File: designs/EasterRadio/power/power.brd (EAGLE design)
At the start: 30.5 x 44.5 mm, 23 parts, among them IC1 MCP73832T-2ACI_OT, IC2 TPS62160DGKR, IC3 DMP1045U-7, J1 10118192-0001LF, J2 S2B-PH-SM4

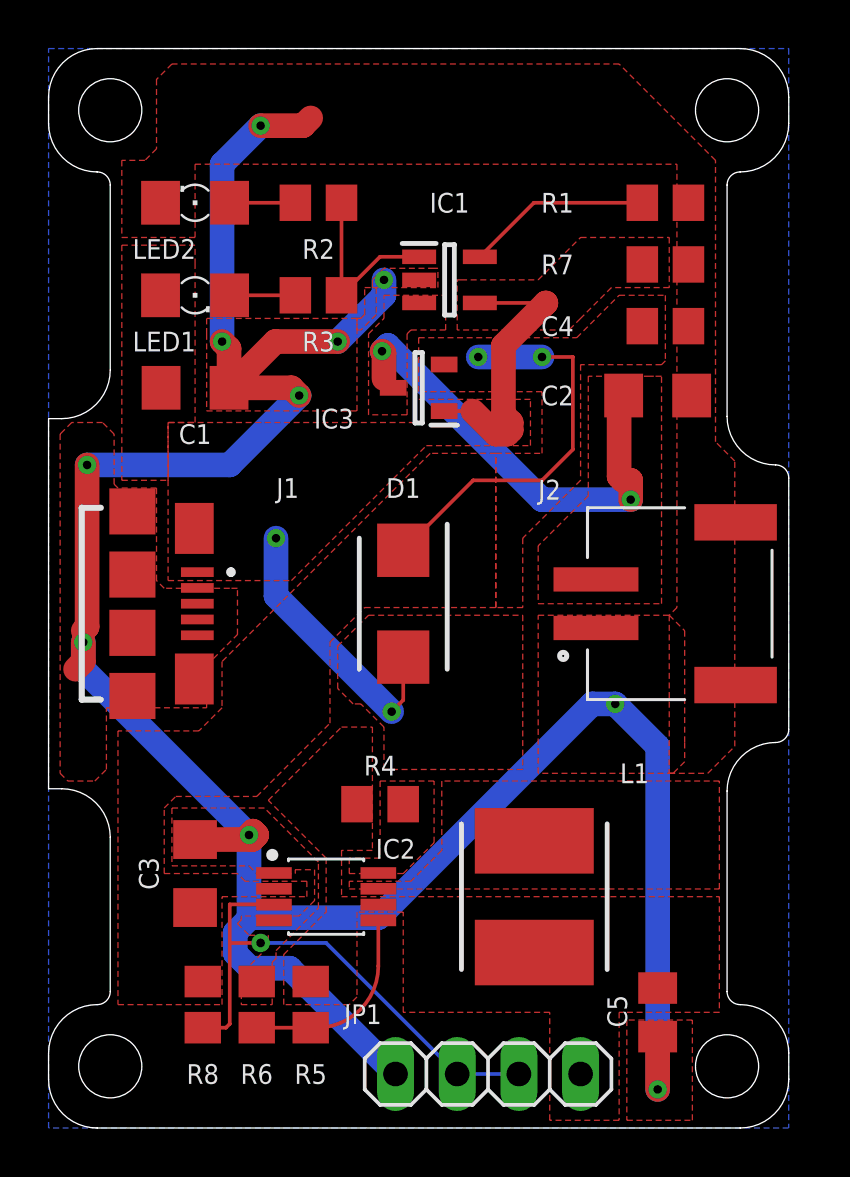
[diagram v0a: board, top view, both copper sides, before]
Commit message: added final power and amplifier design and ESP32 E footprint
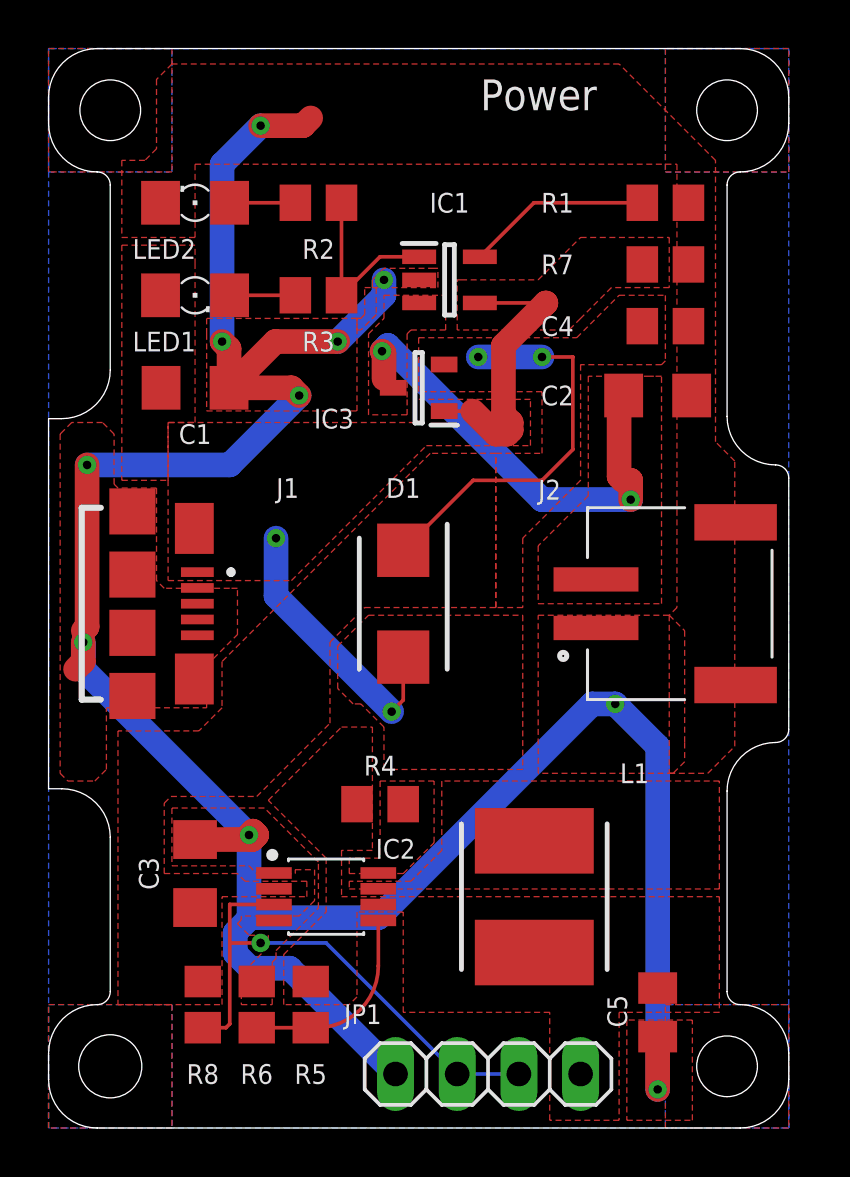
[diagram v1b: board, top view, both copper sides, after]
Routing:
- added copper zone on layer 1, net AGND
- added copper zone on layer 16, net AGND
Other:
- board text added: "Power"
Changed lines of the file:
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@@
 <setting verticaltext="up"/>
 </settings>
-<grid distance="50" unitdist="mil" unit="mil" style="lines" multiple="1" display="yes" altdistance="5" altunitdist="mil" altunit="mil"/>
+<grid distance="0.1" unitdist="mm" unit="mm" style="lines" multiple="1" display="yes" altdistance="5" altunitdist="mil" altunit="mil"/>
 <layers>
 <layer number="1" name="Top" color="4" fill="1" visible="yes" active="yes"/>
@@
 </layers>
 <board>
-<fusionsync huburn="a.cGVyc29uYWw6dWUyYTNmMDU1" projecturn="a.cGVyc29uYWw6dWUyYTNmMDU1IzIwMTgxMjEwMTY0OTQ5MjI2" f3durn="urn:adsk.wipprod:dm.lineage:3cznDv7KT36rVomoCqRWPA" pcbguid="1af594dc-ea54-476d-972d-07e52e169c12" lastpulledtime="" lastsyncedchangeguid="" latestrevisionid="9bc7aa04-2e5e-4955-87e8-cad4fff14e45" lastsyncedrevisionid="9bc7aa04-2e5e-4955-87e8-cad4fff14e45" lastboardhashguid="fae16e1f-5e92-1b48-87bb-c95042e668dd" lastpushedtime="2020-11-09T22:31:19Z" linktopcb3d="true"/>
+<fusionsync huburn="a.cGVyc29uYWw6dWUyYTNmMDU1" projecturn="a.cGVyc29uYWw6dWUyYTNmMDU1IzIwMTgxMjEwMTY0OTQ5MjI2" f3durn="urn:adsk.wipprod:dm.lineage:3cznDv7KT36rVomoCqRWPA" pcbguid="" lastpulledtime="" lastsyncedchangeguid="" latestrevisionid="9bc7aa04-2e5e-4955-87e8-cad4fff14e45" lastsyncedrevisionid="9bc7aa04-2e5e-4955-87e8-cad4fff14e45" lastboardhashguid="fae16e1f-5e92-1b48-87bb-c95042e668dd" lastpushedtime="2020-11-09T22:31:19Z" linktopcb3d="true"/>
 <plain>
-<hole x="2.54" y="41.91" drill="2.6"/>
-<hole x="27.94" y="41.91" drill="2.6"/>
-<hole x="27.94" y="2.54" drill="2.6"/>
+<hole x="2.54" y="41.91" drill="2.5"/>
+<hole x="27.94" y="41.91" drill="2.5"/>
+<hole x="27.94" y="2.54" drill="2.5"/>
 <hole x="2.54" y="2.54" drill="2.6"/>
 <wire x1="2.54" y1="31.21" x2="2.54" y2="38.83" width="0" layer="20"/>
@@
 <wire x1="0" y1="29.21" x2="0.54" y2="29.21" width="0" layer="20"/>
 <wire x1="0.54" y1="29.21" x2="2.54" y2="31.21" width="0" layer="20" curve="90"/>
+<text x="17.78" y="41.91" size="1.27" layer="25">Power</text>
 </plain>
 <attributes>
@@
 <vertex x="7.77875" y="10.4775"/>
 <vertex x="4.7625" y="10.4775"/>
-<vertex x="4.7625" y="13.17625"/>
-<vertex x="5.23875" y="13.6525"/>
+<vertex x="4.7625" y="13.37625"/>
+<vertex x="5.03875" y="13.6525"/>
 <vertex x="8.5725" y="13.6525"/>
 <vertex x="11.58875" y="16.66875"/>
@@
 <wire x1="19.3675" y1="2.2225" x2="16.8275" y2="2.2225" width="0.1524" layer="16"/>
 </signal>
+<signal name="AGND">
+<polygon width="0" layer="1" pour="cutout">
+<vertex x="0" y="5.08"/>
+<vertex x="5.08" y="5.08"/>
+<vertex x="5.08" y="0"/>
+<vertex x="0" y="0"/>
+</polygon>
+<polygon width="0" layer="1" pour="cutout">
+<vertex x="25.4" y="0"/>
+<vertex x="25.4" y="5.08"/>
+<vertex x="30.48" y="5.08"/>
+<vertex x="30.48" y="0"/>
+<vertex x="26.67" y="0"/>
+</polygon>
+<polygon width="0" layer="1" pour="cutout">
+<vertex x="25.4" y="44.45"/>
+<vertex x="25.4" y="39.37"/>
+<vertex x="30.48" y="39.37"/>
+<vertex x="30.48" y="44.45"/>
+</polygon>
+<polygon width="0" layer="1" pour="cutout">
+<vertex x="5.08" y="44.45"/>
+<vertex x="5.08" y="39.37"/>
+<vertex x="0" y="39.37"/>
+<vertex x="0" y="44.45"/>
+</polygon>
+<polygon width="0" layer="16" pour="cutout">
+<vertex x="0" y="40.64"/>
+<vertex x="0" y="39.37"/>
+<vertex x="5.08" y="39.37"/>
+<vertex x="5.08" y="44.45"/>
+<vertex x="0" y="44.45"/>
+</polygon>
+<polygon width="0" layer="16" pour="cutout">
+<vertex x="25.4" y="44.45"/>
+<vertex x="25.4" y="39.37"/>
+<vertex x="30.48" y="39.37"/>
+<vertex x="30.48" y="44.45"/>
+</polygon>
+<polygon width="0" layer="16" pour="cutout">
+<vertex x="25.4" y="5.08"/>
+<vertex x="25.4" y="0"/>
+<vertex x="30.48" y="0"/>
+<vertex x="30.48" y="5.08"/>
+</polygon>
+<polygon width="0" layer="16" pour="cutout">
+<vertex x="0" y="5.08"/>
+<vertex x="5.08" y="5.08"/>
+<vertex x="5.08" y="0"/>
+<vertex x="0" y="0"/>
+</polygon>
+</signal>
 </signals>
 <mfgpreviewcolors>
@@
 <mfgpreviewcolor name="substratecolor" color="0xFF786E46"/>
 </mfgpreviewcolors>
+<errors>
+</errors>
 </board>
 </drawing>

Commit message: everything pushed to fusion
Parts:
- moved C5 2.00 mm to (25.1, 6.76)
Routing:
- net GNDA: track 108.5 -> 110.5 mm
- removed copper zone on layer 1, net AGND
- removed copper zone on layer 16, net AGND
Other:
- board size 30.5 x 44.5 mm -> 31 x 44 mm
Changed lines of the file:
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@@
 <setting verticaltext="up"/>
 </settings>
-<grid distance="0.1" unitdist="mm" unit="mm" style="lines" multiple="1" display="yes" altdistance="5" altunitdist="mil" altunit="mil"/>
+<grid distance="1" unitdist="mm" unit="mm" style="lines" multiple="1" display="yes" altdistance="5" altunitdist="mil" altunit="mil"/>
 <layers>
 <layer number="1" name="Top" color="4" fill="1" visible="yes" active="yes"/>
@@
 <layer number="27" name="tValues" color="7" fill="1" visible="yes" active="yes"/>
 <layer number="28" name="bValues" color="7" fill="1" visible="yes" active="yes"/>
-<layer number="29" name="tStop" color="7" fill="3" visible="no" active="yes"/>
+<layer number="29" name="tStop" color="7" fill="3" visible="yes" active="yes"/>
 <layer number="30" name="bStop" color="7" fill="6" visible="no" active="yes"/>
 <layer number="31" name="tCream" color="7" fill="4" visible="no" active="yes"/>
@@
 <fusionsync huburn="a.cGVyc29uYWw6dWUyYTNmMDU1" projecturn="a.cGVyc29uYWw6dWUyYTNmMDU1IzIwMTgxMjEwMTY0OTQ5MjI2" f3durn="urn:adsk.wipprod:dm.lineage:3cznDv7KT36rVomoCqRWPA" pcbguid="" lastpulledtime="" lastsyncedchangeguid="" latestrevisionid="9bc7aa04-2e5e-4955-87e8-cad4fff14e45" lastsyncedrevisionid="9bc7aa04-2e5e-4955-87e8-cad4fff14e45" lastboardhashguid="fae16e1f-5e92-1b48-87bb-c95042e668dd" lastpushedtime="2020-11-09T22:31:19Z" linktopcb3d="true"/>
 <plain>
-<hole x="2.54" y="41.91" drill="2.5"/>
-<hole x="27.94" y="41.91" drill="2.5"/>
-<hole x="27.94" y="2.54" drill="2.5"/>
-<hole x="2.54" y="2.54" drill="2.6"/>
-<wire x1="2.54" y1="31.21" x2="2.54" y2="38.83" width="0" layer="20"/>
-<wire x1="2.54" y1="38.83" x2="2" y2="39.37" width="0" layer="20" curve="90"/>
-<wire x1="2" y1="39.37" x2="0" y2="41.37" width="0" layer="20" curve="-90"/>
-<wire x1="0" y1="41.37" x2="0" y2="42.45" width="0" layer="20"/>
-<wire x1="0" y1="42.45" x2="2" y2="44.45" width="0" layer="20" curve="-90"/>
-<wire x1="2" y1="44.45" x2="28.48" y2="44.45" width="0" layer="20"/>
-<wire x1="28.48" y1="44.45" x2="30.48" y2="42.45" width="0" layer="20" curve="-90"/>
-<wire x1="30.48" y1="42.45" x2="30.48" y2="41.37" width="0" layer="20"/>
-<wire x1="30.48" y1="41.37" x2="28.48" y2="39.37" width="0" layer="20" curve="-90"/>
-<wire x1="28.48" y1="39.37" x2="27.94" y2="38.83" width="0" layer="20" curve="90"/>
-<wire x1="27.94" y1="38.83" x2="27.94" y2="29.305" width="0" layer="20"/>
-<wire x1="27.94" y1="29.305" x2="29.94" y2="27.305" width="0" layer="20" curve="90"/>
-<wire x1="29.94" y1="27.305" x2="30.48" y2="26.765" width="0" layer="20" curve="-90"/>
-<wire x1="30.48" y1="26.765" x2="30.48" y2="16.415" width="0" layer="20"/>
-<wire x1="30.48" y1="16.415" x2="29.94" y2="15.875" width="0" layer="20" curve="-90"/>
-<wire x1="29.94" y1="15.875" x2="27.94" y2="13.875" width="0" layer="20" curve="90"/>
-<wire x1="27.94" y1="13.875" x2="27.94" y2="5.62" width="0" layer="20"/>
-<wire x1="27.94" y1="5.62" x2="28.48" y2="5.08" width="0" layer="20" curve="90"/>
-<wire x1="28.48" y1="5.08" x2="30.48" y2="3.08" width="0" layer="20" curve="-90"/>
-<wire x1="30.48" y1="3.08" x2="30.48" y2="2" width="0" layer="20"/>
-<wire x1="30.48" y1="2" x2="28.48" y2="0" width="0" layer="20" curve="-90"/>
-<wire x1="28.48" y1="0" x2="2" y2="0" width="0" layer="20"/>
-<wire x1="2" y1="0" x2="0" y2="2" width="0" layer="20" curve="-90"/>
-<wire x1="0" y1="2" x2="0" y2="3.08" width="0" layer="20"/>
-<wire x1="0" y1="3.08" x2="2" y2="5.08" width="0" layer="20" curve="-90"/>
-<wire x1="2" y1="5.08" x2="2.54" y2="5.62" width="0" layer="20" curve="90"/>
-<wire x1="2.54" y1="5.62" x2="2.54" y2="11.97" width="0" layer="20"/>
-<wire x1="2.54" y1="11.97" x2="0.54" y2="13.97" width="0" layer="20" curve="90"/>
-<wire x1="0.54" y1="13.97" x2="0" y2="13.97" width="0" layer="20"/>
-<wire x1="0" y1="13.97" x2="0" y2="29.21" width="0" layer="20"/>
-<wire x1="0" y1="29.21" x2="0.54" y2="29.21" width="0" layer="20"/>
-<wire x1="0.54" y1="29.21" x2="2.54" y2="31.21" width="0" layer="20" curve="90"/>
-<text x="17.78" y="41.91" size="1.27" layer="25">Power</text>
+<text x="14.78" y="41.91" size="1.778" layer="29" font="vector" ratio="15" align="center-left">Power</text>
+<wire x1="29" y1="44" x2="2" y2="44" width="0" layer="20"/>
+<wire x1="2" y1="44" x2="0" y2="42" width="0" layer="20"/>
+<wire x1="0" y1="42" x2="0" y2="2" width="0" layer="20"/>
+<wire x1="0" y1="2" x2="2" y2="0" width="0" layer="20"/>
+<wire x1="2" y1="0" x2="29" y2="0" width="0" layer="20"/>
+<wire x1="29" y1="0" x2="31" y2="2" width="0" layer="20"/>
+<wire x1="31" y1="2" x2="31" y2="42" width="0" layer="20"/>
+<wire x1="31" y1="42" x2="29" y2="44" width="0" layer="20"/>
+<text x="14.78" y="41.91" size="1.778" layer="1" font="vector" ratio="15" align="center-left">Power</text>
+<hole x="3" y="41" drill="2.8"/>
+<hole x="28" y="41" drill="2.8"/>
+<hole x="28" y="3" drill="2.8"/>
+<hole x="3" y="3" drill="2.8"/>
+<circle x="3" y="3" radius="1" width="2.54" layer="41"/>
+<circle x="28" y="3" radius="1" width="2.54" layer="41"/>
+<circle x="28" y="41" radius="1.4142125" width="2.54" layer="41"/>
+<circle x="3" y="41" radius="1" width="2.54" layer="41"/>
 </plain>
 <attributes>
@@
 <attribute name="SPICEPREFIX" value="C" x="40.3225" y="54.9275" size="1.778" layer="27" rot="R90" display="off"/>
 </element>
-<element name="C5" library="MouserUseful" package="C0805K" package3d_urn="urn:adsk.eagle:package:23681/2" value="22uF" x="25.0825" y="4.7625" smashed="yes" rot="R270">
-<attribute name="MAXV" value="16V" x="-15.5575" y="-20.6375" size="1.778" layer="27" rot="R270" display="off"/>
-<attribute name="NAME" x="23.4175" y="4.81" size="0.8128" layer="25" rot="R270" align="center"/>
-<attribute name="POPULARITY" value="52" x="-15.5575" y="-20.6375" size="1.778" layer="27" rot="R270" display="off"/>
-<attribute name="SPICEPREFIX" value="C" x="-15.5575" y="-20.6375" size="1.778" layer="27" rot="R270" display="off"/>
+<element name="C5" library="MouserUseful" package="C0805K" package3d_urn="urn:adsk.eagle:package:23681/2" value="22uF" x="25.0825" y="6.7625" smashed="yes" rot="R270">
+<attribute name="MAXV" value="16V" x="-15.5575" y="-18.6375" size="1.778" layer="27" rot="R270" display="off"/>
+<attribute name="NAME" x="23.4175" y="6.81" size="0.8128" layer="25" rot="R270" align="center"/>
+<attribute name="POPULARITY" value="52" x="-15.5575" y="-18.6375" size="1.778" layer="27" rot="R270" display="off"/>
+<attribute name="SPICEPREFIX" value="C" x="-15.5575" y="-18.6375" size="1.778" layer="27" rot="R270" display="off"/>
 </element>
 <element name="C2" library="CommonParts" package="C1206" package3d_urn="urn:adsk.eagle:package:23618/2" value="4.7uF" x="25.0825" y="30.1625" smashed="yes" rot="R180">
@@
 </polygon>
 <polygon width="0.1524" layer="1">
-<vertex x="23.8125" y="4.445"/>
+<vertex x="23.8125" y="6.445"/>
 <vertex x="23.8125" y="0.3175"/>
 <vertex x="26.51125" y="0.3175"/>
-<vertex x="26.51125" y="4.445"/>
+<vertex x="26.51125" y="6.445"/>
 </polygon>
 <polygon width="0.1524" layer="1">
@@
 <wire x1="23.33625" y1="17.4625" x2="25.0825" y2="15.71625" width="1.016" layer="16"/>
 <via x="25.0825" y="1.5875" extent="1-16" drill="0.35"/>
-<wire x1="25.0825" y1="1.5875" x2="25.0825" y2="3.7625" width="1.016" layer="1"/>
+<wire x1="25.0825" y1="1.5875" x2="25.0825" y2="5.7625" width="1.016" layer="1"/>
 <wire x1="25.0825" y1="15.71625" x2="25.0825" y2="1.5875" width="1.016" layer="16"/>
 <polygon width="0" layer="16">
-<vertex x="0" y="44.45"/>
-<vertex x="30.48" y="44.45"/>
-<vertex x="30.48" y="0"/>
-<vertex x="0" y="0"/>
+<vertex x="0" y="2"/>
+<vertex x="0" y="42"/>
+<vertex x="2" y="44"/>
+<vertex x="29" y="44"/>
+<vertex x="31" y="42"/>
+<vertex x="31" y="2"/>
+<vertex x="29" y="0"/>
+<vertex x="2" y="0"/>
 </polygon>
 </signal>
@@
 <vertex x="12.065" y="9.525"/>
 <vertex x="27.6225" y="9.525"/>
-<vertex x="27.6225" y="4.7625"/>
-<vertex x="23.495" y="4.7625"/>
+<vertex x="27.6225" y="6.7625"/>
+<vertex x="23.495" y="6.7625"/>
 <vertex x="23.495" y="0.3175"/>
 <vertex x="20.6375" y="0.3175"/>
@@
 <wire x1="19.3675" y1="2.2225" x2="16.8275" y2="2.2225" width="0.1524" layer="16"/>
 </signal>
-<signal name="AGND">
-<polygon width="0" layer="1" pour="cutout">
-<vertex x="0" y="5.08"/>
-<vertex x="5.08" y="5.08"/>
-<vertex x="5.08" y="0"/>
-<vertex x="0" y="0"/>
-</polygon>
-<polygon width="0" layer="1" pour="cutout">
-<vertex x="25.4" y="0"/>
-<vertex x="25.4" y="5.08"/>
-<vertex x="30.48" y="5.08"/>
-<vertex x="30.48" y="0"/>
-<vertex x="26.67" y="0"/>
-</polygon>
-<polygon width="0" layer="1" pour="cutout">
-<vertex x="25.4" y="44.45"/>
-<vertex x="25.4" y="39.37"/>
-<vertex x="30.48" y="39.37"/>
-<vertex x="30.48" y="44.45"/>
-</polygon>
-<polygon width="0" layer="1" pour="cutout">
-<vertex x="5.08" y="44.45"/>
-<vertex x="5.08" y="39.37"/>
-<vertex x="0" y="39.37"/>
-<vertex x="0" y="44.45"/>
-</polygon>
-<polygon width="0" layer="16" pour="cutout">
-<vertex x="0" y="40.64"/>
-<vertex x="0" y="39.37"/>
-<vertex x="5.08" y="39.37"/>
-<vertex x="5.08" y="44.45"/>
-<vertex x="0" y="44.45"/>
-</polygon>
-<polygon width="0" layer="16" pour="cutout">
-<vertex x="25.4" y="44.45"/>
-<vertex x="25.4" y="39.37"/>
-<vertex x="30.48" y="39.37"/>
-<vertex x="30.48" y="44.45"/>
-</polygon>
-<polygon width="0" layer="16" pour="cutout">
-<vertex x="25.4" y="5.08"/>
-<vertex x="25.4" y="0"/>
-<vertex x="30.48" y="0"/>
-<vertex x="30.48" y="5.08"/>
-</polygon>
-<polygon width="0" layer="16" pour="cutout">
-<vertex x="0" y="5.08"/>
-<vertex x="5.08" y="5.08"/>
-<vertex x="5.08" y="0"/>
-<vertex x="0" y="0"/>
-</polygon>
-</signal>
 </signals>
